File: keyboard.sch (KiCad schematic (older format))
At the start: 98 parts, among them SW1 cheery_mx_switch_led, SW10 cheery_mx_switch_led, SW11 cheery_mx_switch_led, SW12 cheery_mx_switch_led, SW13 cheery_mx_switch_led, SW14 cheery_mx_switch_led, SW15 cheery_mx_switch_led, SW16 cheery_mx_switch_led, SW17 cheery_mx_switch_led, SW18 cheery_mx_switch_led, SW19 cheery_mx_switch_led, SW2 cheery_mx_switch_led, SW20 cheery_mx_switch_led, SW21 cheery_mx_switch_led, SW22 cheery_mx_switch_led, SW23 cheery_mx_switch_led, SW24 cheery_mx_switch_led, SW25 cheery_mx_switch_led, SW26 cheery_mx_switch_led, SW27 cheery_mx_switch_led, SW28 cheery_mx_switch_led, SW29 cheery_mx_switch_led, SW3 cheery_mx_switch_led, SW30 cheery_mx_switch_led, SW31 cheery_mx_switch_led, SW32 cheery_mx_switch_led, SW33 cheery_mx_switch_led, SW34 cheery_mx_switch_led, SW35 cheery_mx_switch_led, SW36 cheery_mx_switch_led, SW37 cheery_mx_switch_led, SW38 cheery_mx_switch_led, SW39 cheery_mx_switch_led, SW4 cheery_mx_switch_led, SW40 cheery_mx_switch_led, SW5 cheery_mx_switch_led, SW6 cheery_mx_switch_led, SW7 cheery_mx_switch_led, SW8 cheery_mx_switch_led, SW9 cheery_mx_switch_led, U3 74HC595, U4 74HC595, U5 74HC595

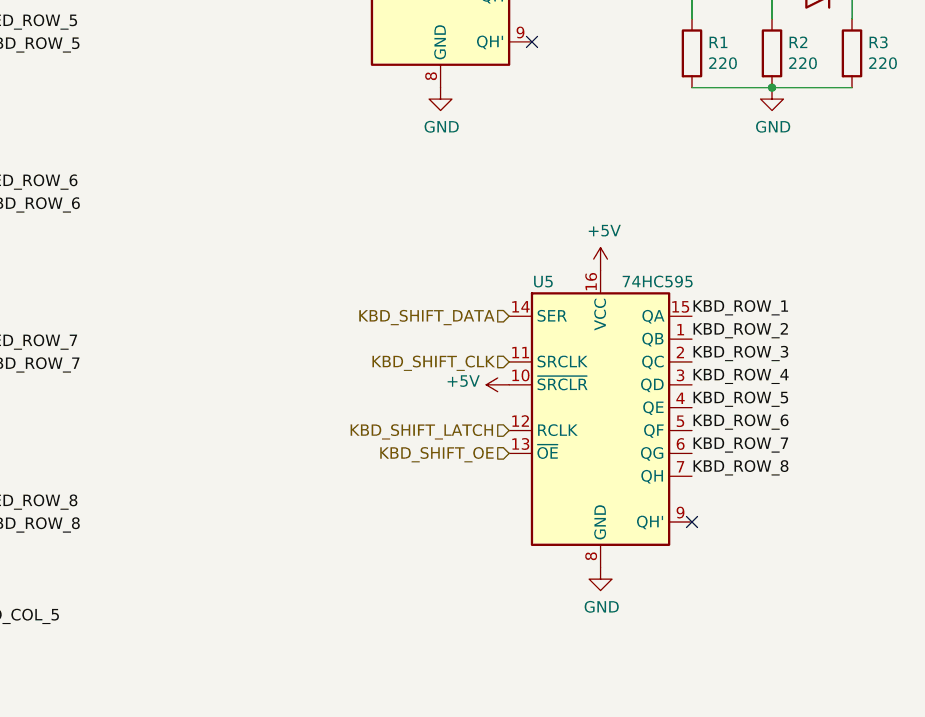
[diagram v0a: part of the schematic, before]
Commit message: atmega128 and external memory
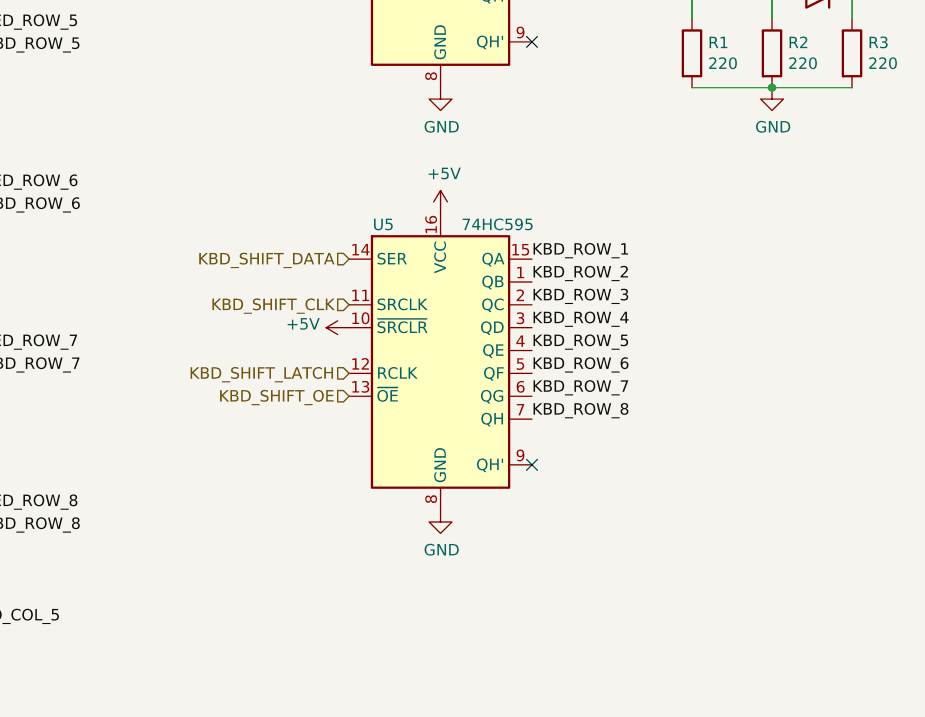
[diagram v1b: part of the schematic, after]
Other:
- moved on the sheet: U5
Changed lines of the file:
@@
 $Descr A4 11693 8268
 encoding utf-8
-Sheet 2 2
+Sheet 2 3
 Title ""
 Date ""
@@
 L 74xx:74HC595 U5
 U 1 1 60951861
-P 9850 5550
-F 0 "U5" H 9600 6100 50  0000 C CNN
-F 1 "74HC595" H 10100 6100 50  0000 C CNN
-F 2 "Package_DIP:DIP-16_W7.62mm" H 9850 5550 50  0001 C CNN
-F 3 "http://www.ti.com/lit/ds/symlink/sn74hc595.pdf" H 9850 5550 50  0001 C CNN
-	1    9850 5550
+P 9150 5300
+F 0 "U5" H 8900 5850 50  0000 C CNN
+F 1 "74HC595" H 9400 5850 50  0000 C CNN
+F 2 "Package_DIP:DIP-16_W7.62mm" H 9150 5300 50  0001 C CNN
+F 3 "http://www.ti.com/lit/ds/symlink/sn74hc595.pdf" H 9150 5300 50  0001 C CNN
+	1    9150 5300
 	1    0    0    -1
 $EndComp
@@
 KBD_COL_5
 $Comp
-L power:GND #PWR03
+L power:GND #PWR0113
 U 1 1 60EC0B77
 P 9150 2300
-F 0 "#PWR03" H 9150 2050 50  0001 C CNN
+F 0 "#PWR0113" H 9150 2050 50  0001 C CNN
 F 1 "GND" H 9155 2127 50  0000 C CNN
 F 2 "" H 9150 2300 50  0001 C CNN
@@
 L power:GND #PWR011
 U 1 1 60EC545F
-P 9850 6250
-F 0 "#PWR011" H 9850 6000 50  0001 C CNN
-F 1 "GND" H 9855 6077 50  0000 C CNN
-F 2 "" H 9850 6250 50  0001 C CNN
-F 3 "" H 9850 6250 50  0001 C CNN
-	1    9850 6250
+P 9150 6000
+F 0 "#PWR011" H 9150 5750 50  0001 C CNN
+F 1 "GND" H 9155 5827 50  0000 C CNN
+F 2 "" H 9150 6000 50  0001 C CNN
+F 3 "" H 9150 6000 50  0001 C CNN
+	1    9150 6000
 	1    0    0    -1
 $EndComp
@@
 L power:+5V #PWR08
 U 1 1 60ED3965
-P 9850 4950
-F 0 "#PWR08" H 9850 4800 50  0001 C CNN
-F 1 "+5V" H 9865 5123 50  0000 C CNN
-F 2 "" H 9850 4950 50  0001 C CNN
-F 3 "" H 9850 4950 50  0001 C CNN
-	1    9850 4950
-	1    0    0    -1
-$EndComp
-$Comp
-L power:+5V #PWR04
+P 9150 4700
+F 0 "#PWR08" H 9150 4550 50  0001 C CNN
+F 1 "+5V" H 9165 4873 50  0000 C CNN
+F 2 "" H 9150 4700 50  0001 C CNN
+F 3 "" H 9150 4700 50  0001 C CNN
+	1    9150 4700
+	1    0    0    -1
+$EndComp
+$Comp
+L power:+5V #PWR0114
 U 1 1 60ED4B55
 P 9150 2850
-F 0 "#PWR04" H 9150 2700 50  0001 C CNN
+F 0 "#PWR0114" H 9150 2700 50  0001 C CNN
 F 1 "+5V" H 9165 3023 50  0000 C CNN
 F 2 "" H 9150 2850 50  0001 C CNN
@@
 $EndComp
 $Comp
-L power:+5V #PWR01
+L power:+5V #PWR0115
 U 1 1 60ED750D
 P 9150 1000
-F 0 "#PWR01" H 9150 850 50  0001 C CNN
+F 0 "#PWR0115" H 9150 850 50  0001 C CNN
 F 1 "+5V" H 9165 1173 50  0000 C CNN
 F 2 "" H 9150 1000 50  0001 C CNN
@@
 	8200 3250 8750 3250
 $Comp
-L power:+5V #PWR02
+L power:+5V #PWR0116
 U 1 1 6181B807
 P 8750 1500
-F 0 "#PWR02" H 8750 1350 50  0001 C CNN
+F 0 "#PWR0116" H 8750 1350 50  0001 C CNN
 F 1 "+5V" V 8765 1628 50  0000 L CNN
 F 2 "" H 8750 1500 50  0001 C CNN
@@
 Text HLabel 8750 1200 0    50   Input ~ 0
 LED_SHIFT_DATA
-Text Label 10250 5150 0    50   ~ 0
+Text Label 9550 4900 0    50   ~ 0
 KBD_ROW_1
-Text Label 10250 5250 0    50   ~ 0
+Text Label 9550 5000 0    50   ~ 0
 KBD_ROW_2
-Text Label 10250 5350 0    50   ~ 0
+Text Label 9550 5100 0    50   ~ 0
 KBD_ROW_3
-Text Label 10250 5450 0    50   ~ 0
+Text Label 9550 5200 0    50   ~ 0
 KBD_ROW_4
-Text Label 10250 5550 0    50   ~ 0
+Text Label 9550 5300 0    50   ~ 0
 KBD_ROW_5
-Text Label 10250 5650 0    50   ~ 0
+Text Label 9550 5400 0    50   ~ 0
 KBD_ROW_6
-Text Label 10250 5750 0    50   ~ 0
+Text Label 9550 5500 0    50   ~ 0
 KBD_ROW_7
-Text Label 10250 5850 0    50   ~ 0
+Text Label 9550 5600 0    50   ~ 0
 KBD_ROW_8
-Text HLabel 9450 5150 0    50   Input ~ 0
+Text HLabel 8750 4900 0    50   Input ~ 0
 KBD_SHIFT_DATA
-Text HLabel 9450 5350 0    50   Input ~ 0
+Text HLabel 8750 5100 0    50   Input ~ 0
 KBD_SHIFT_CLK
-Text HLabel 9450 5650 0    50   Input ~ 0
+Text HLabel 8750 5400 0    50   Input ~ 0
 KBD_SHIFT_LATCH
-Text HLabel 9450 5750 0    50   Input ~ 0
+Text HLabel 8750 5500 0    50   Input ~ 0
 KBD_SHIFT_OE
 $Comp
 L power:+5V #PWR09
 U 1 1 619BAC7F
-P 9450 5450
-F 0 "#PWR09" H 9450 5300 50  0001 C CNN
-F 1 "+5V" V 9465 5578 50  0000 L CNN
-F 2 "" H 9450 5450 50  0001 C CNN
-F 3 "" H 9450 5450 50  0001 C CNN
-	1    9450 5450
+P 8750 5200
+F 0 "#PWR09" H 8750 5050 50  0001 C CNN
+F 1 "+5V" V 8765 5328 50  0000 L CNN
+F 2 "" H 8750 5200 50  0001 C CNN
+F 3 "" H 8750 5200 50  0001 C CNN
+	1    8750 5200
 	0    -1   -1   0
 $EndComp
-NoConn ~ 10250 6050
+NoConn ~ 9550 5800
 NoConn ~ 9550 3950
 $Comp

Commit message: route icsp and reset button for MMI MCU
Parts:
- SW1, SW10, SW11, SW12, SW13, SW14, SW15, SW16, SW17, SW18, SW19, SW2, SW20, SW21, SW22, SW23, SW24, SW25, SW26, SW27, SW28, SW29, SW3, SW30, SW31, SW32, SW33, SW34, SW35, SW36, SW37, SW38, SW39, SW4, SW40, SW5, SW6, SW7, SW8, SW9: symbol stm_sbc_symbols:cheery_mx_switch_led -> avr_sbc-rescue:cheery_mx_switch_led-stm_sbc_symbols
